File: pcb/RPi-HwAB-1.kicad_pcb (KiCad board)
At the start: 6 copper layers, 65 x 56 mm, 110 parts, among them J1 GPIO, J2 Hirose_FH12-16S, J3 TC2030, M1V0 TestPoint, M1V2 TestPoint, U1 CAT24C256, U2 ADP5054, U3 INA230AIRGTT, U4 MCP9804_DFN, U5 XC7A35T-FGG484, U6 INA230AIRGTT, U8 MX25L3233FZN

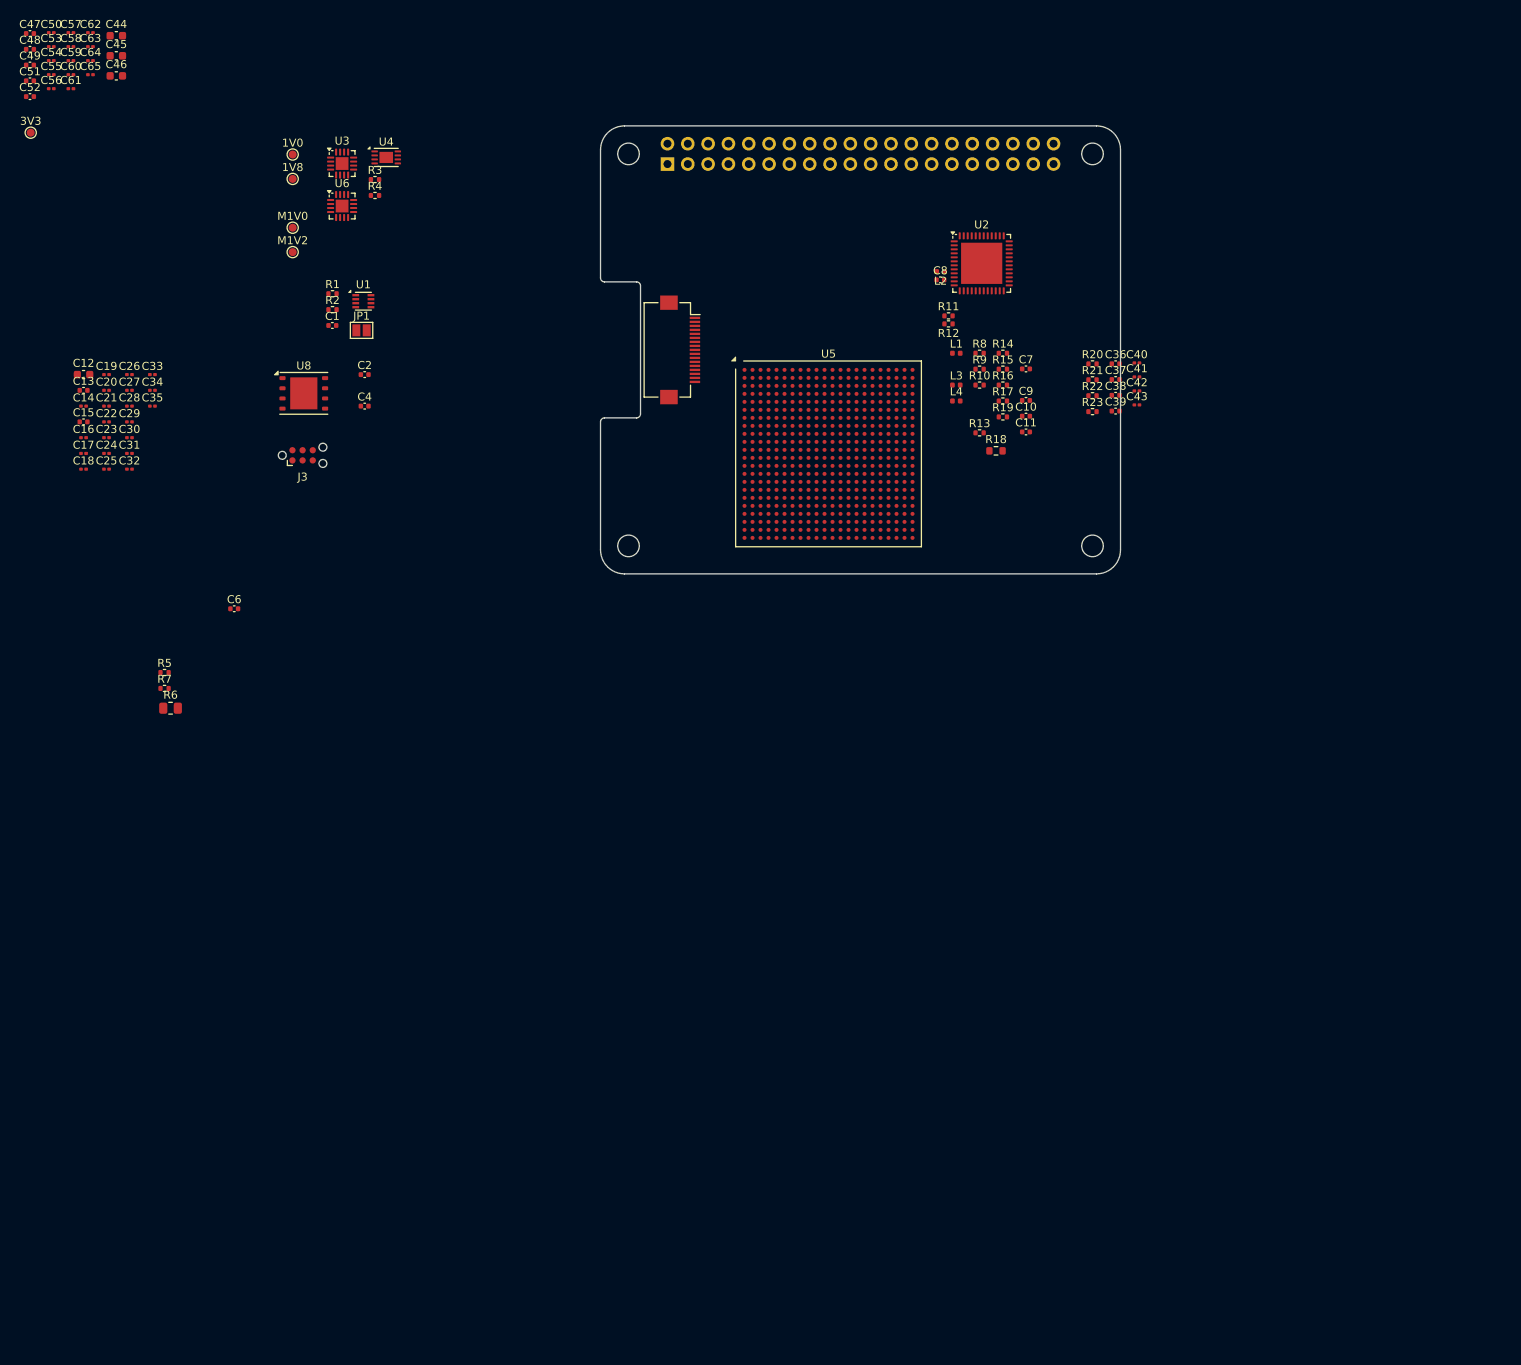
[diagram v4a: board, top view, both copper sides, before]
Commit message: defined memory pinouts
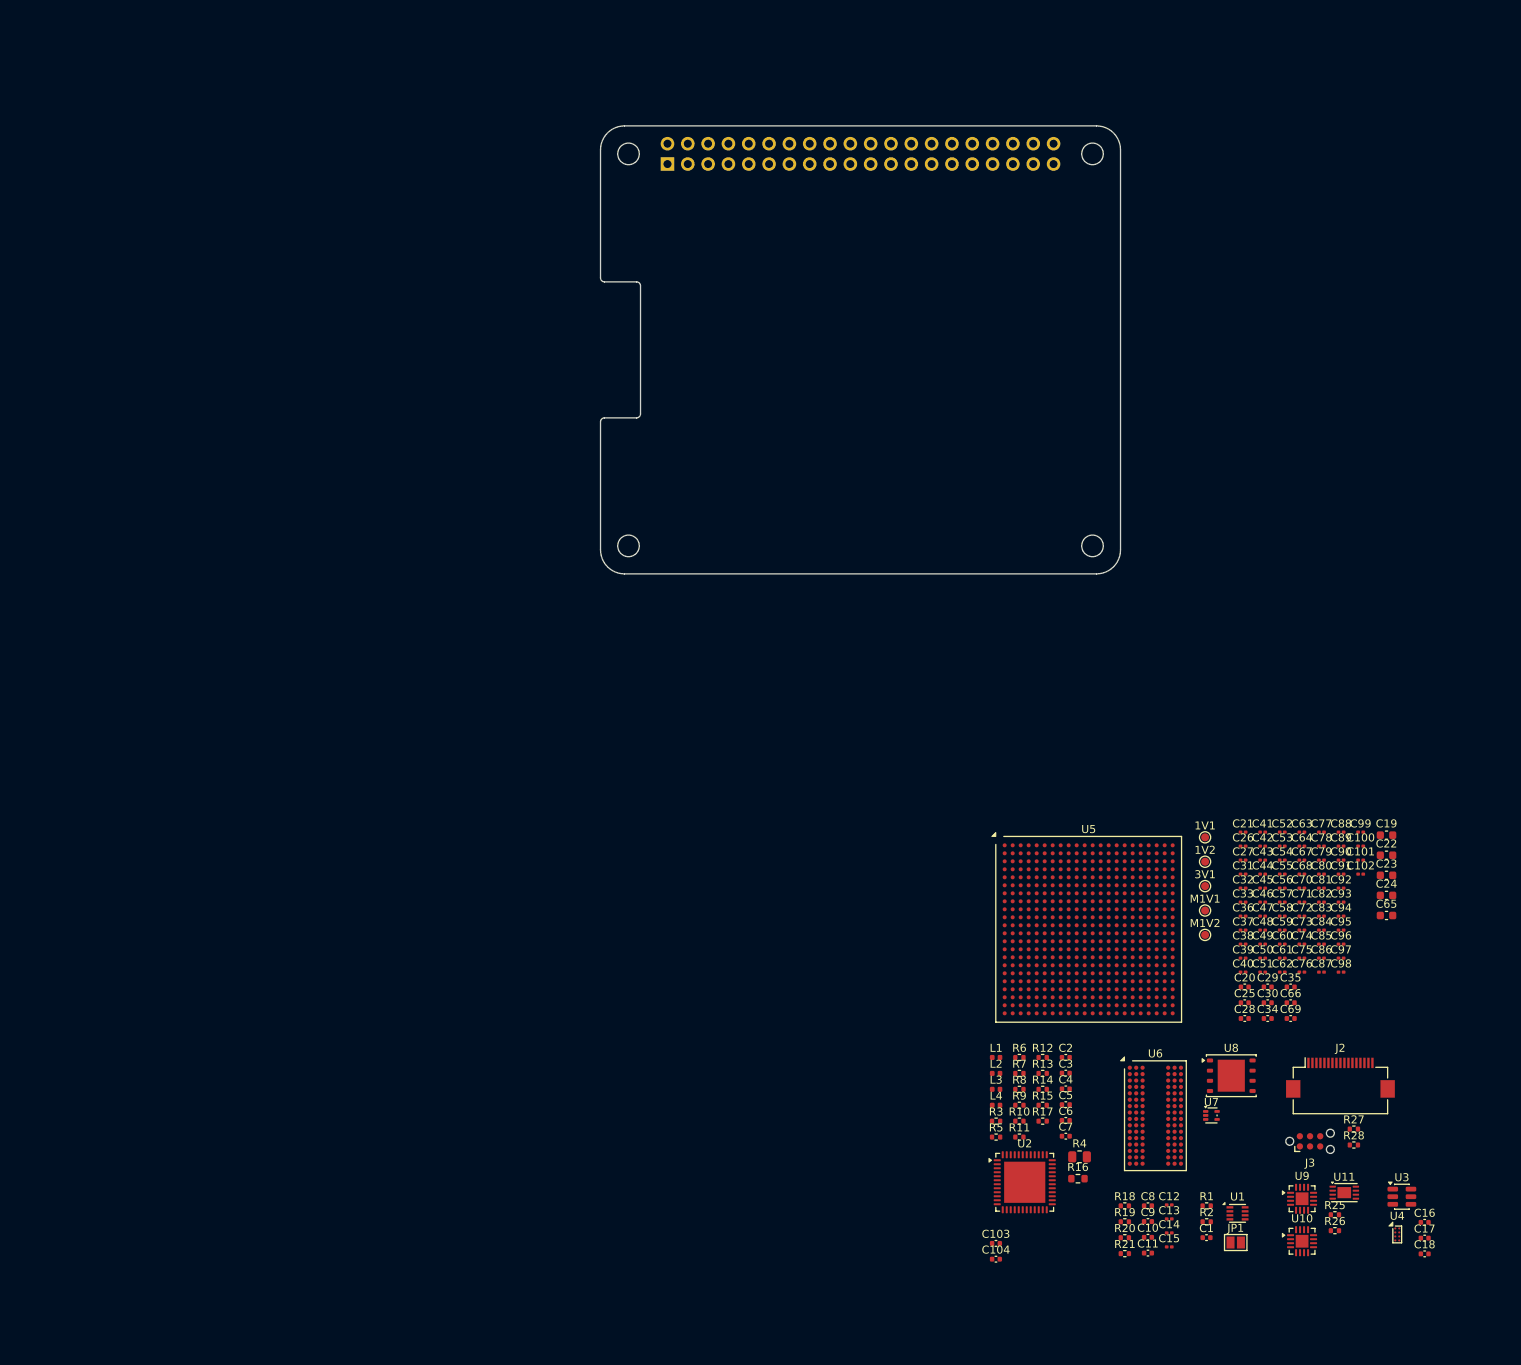
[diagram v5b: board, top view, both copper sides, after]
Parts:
- removed 1V0, 1V8, 3V3, M1V0: TestPoint, TestPoint:TestPoint_Pad_D1.0mm
- removed R22, R23: 10K, Resistor_SMD:R_0402_1005Metric
- added 1V1: TestPoint, TestPoint:TestPoint_Pad_D1.0mm, F.Cu at (175.6, 132.9)
- added 1V2: TestPoint, TestPoint:TestPoint_Pad_D1.0mm, F.Cu at (175.6, 136.0)
- added 3V1: TestPoint, TestPoint:TestPoint_Pad_D1.0mm, F.Cu at (175.6, 139.0)
- added C100: 0.1uF, Capacitor_SMD:C_0201_0603Metric, F.Cu at (195.0, 134.0)
- added C101: 0.1uF, Capacitor_SMD:C_0201_0603Metric, F.Cu at (195.0, 135.8)
- added C102: 0.1uF, Capacitor_SMD:C_0201_0603Metric, F.Cu at (195.0, 137.5)
- added C103: 0.1uF, Capacitor_SMD:C_0402_1005Metric, F.Cu at (149.4, 183.7)
- added C104: 0.1uF, Capacitor_SMD:C_0402_1005Metric, F.Cu at (149.4, 185.7)
- added C3: 0.1uF, Capacitor_SMD:C_0402_1005Metric, F.Cu at (158.2, 162.4)
- added C5: 0.1uF, Capacitor_SMD:C_0402_1005Metric, F.Cu at (158.2, 166.3)
- added C66: 0.1uF, Capacitor_SMD:C_0402_1005Metric, F.Cu at (186.3, 153.6)
- added C67: 0.1uF, Capacitor_SMD:C_0201_0603Metric, F.Cu at (187.7, 135.8)
- added C68: 0.1uF, Capacitor_SMD:C_0201_0603Metric, F.Cu at (187.7, 137.5)
- added C69: 10uF, Capacitor_SMD:C_0402_1005Metric, F.Cu at (186.3, 155.6)
- added C70: 0.1uF, Capacitor_SMD:C_0201_0603Metric, F.Cu at (187.7, 139.3)
- added C71: 0.1uF, Capacitor_SMD:C_0201_0603Metric, F.Cu at (187.7, 141.0)
- added C72: 0.1uF, Capacitor_SMD:C_0201_0603Metric, F.Cu at (187.7, 142.8)
- added C73: 0.1uF, Capacitor_SMD:C_0201_0603Metric, F.Cu at (187.7, 144.5)
- added C74: 0.1uF, Capacitor_SMD:C_0201_0603Metric, F.Cu at (187.7, 146.3)
- added C75: 0.1uF, Capacitor_SMD:C_0201_0603Metric, F.Cu at (187.7, 148.0)
- added C76: 0.1uF, Capacitor_SMD:C_0201_0603Metric, F.Cu at (187.7, 149.8)
- added C77: 0.1uF, Capacitor_SMD:C_0201_0603Metric, F.Cu at (190.1, 132.3)
- added C78: 0.1uF, Capacitor_SMD:C_0201_0603Metric, F.Cu at (190.1, 134.0)
- added C79: 0.1uF, Capacitor_SMD:C_0201_0603Metric, F.Cu at (190.1, 135.8)
- added C80: 0.1uF, Capacitor_SMD:C_0201_0603Metric, F.Cu at (190.1, 137.5)
- added C81: 0.1uF, Capacitor_SMD:C_0201_0603Metric, F.Cu at (190.1, 139.3)
- added C82: 0.1uF, Capacitor_SMD:C_0201_0603Metric, F.Cu at (190.1, 141.0)
- added C83: 0.1uF, Capacitor_SMD:C_0201_0603Metric, F.Cu at (190.1, 142.8)
- added C84: 0.1uF, Capacitor_SMD:C_0201_0603Metric, F.Cu at (190.1, 144.5)
- added C85: 0.1uF, Capacitor_SMD:C_0201_0603Metric, F.Cu at (190.1, 146.3)
- added C86: 0.1uF, Capacitor_SMD:C_0201_0603Metric, F.Cu at (190.1, 148.0)
- added C87: 0.1uF, Capacitor_SMD:C_0201_0603Metric, F.Cu at (190.1, 149.8)
- added C88: 0.1uF, Capacitor_SMD:C_0201_0603Metric, F.Cu at (192.6, 132.3)
- added C89: 0.1uF, Capacitor_SMD:C_0201_0603Metric, F.Cu at (192.6, 134.0)
- added C90: 0.1uF, Capacitor_SMD:C_0201_0603Metric, F.Cu at (192.6, 135.8)
- added C91: 0.1uF, Capacitor_SMD:C_0201_0603Metric, F.Cu at (192.6, 137.5)
- added C92: 0.1uF, Capacitor_SMD:C_0201_0603Metric, F.Cu at (192.6, 139.3)
- added C93: 0.1uF, Capacitor_SMD:C_0201_0603Metric, F.Cu at (192.6, 141.0)
- added C94: 0.1uF, Capacitor_SMD:C_0201_0603Metric, F.Cu at (192.6, 142.8)
- added C95: 0.1uF, Capacitor_SMD:C_0201_0603Metric, F.Cu at (192.6, 144.5)
- added C96: 0.1uF, Capacitor_SMD:C_0201_0603Metric, F.Cu at (192.6, 146.3)
- added C97: 0.1uF, Capacitor_SMD:C_0201_0603Metric, F.Cu at (192.6, 148.0)
- added C98: 0.1uF, Capacitor_SMD:C_0201_0603Metric, F.Cu at (192.6, 149.8)
- added C99: 0.1uF, Capacitor_SMD:C_0201_0603Metric, F.Cu at (195.0, 132.3)
- added M1V1: TestPoint, TestPoint:TestPoint_Pad_D1.0mm, F.Cu at (175.6, 142.1)
- added R25: 4.7K, Resistor_SMD:R_0402_1005Metric, F.Cu at (191.8, 180.1)
- added R26: 4.7K, Resistor_SMD:R_0402_1005Metric, F.Cu at (191.8, 182.1)
- added R27: 100K, Resistor_SMD:R_0402_1005Metric, F.Cu at (194.2, 169.4)
- added R28: 2.2K, Resistor_SMD:R_0402_1005Metric, F.Cu at (194.2, 171.4)
- added U10: INA230AIRGTT, Package_DFN_QFN:VQFN-16-1EP_3x3mm_P0.5mm_EP1.6x1.6mm, F.Cu at (187.7, 183.4)
- added U11: MCP9804_DFN, Package_DFN_QFN:DFN-8-1EP_3x2mm_P0.5mm_EP1.7x1.4mm, F.Cu at (193.0, 177.3)
- added U7: TCR2EE135, Package_TO_SOT_SMD:SOT-553, F.Cu at (176.4, 167.7)
- added U9: INA230AIRGTT, Package_DFN_QFN:VQFN-16-1EP_3x3mm_P0.5mm_EP1.6x1.6mm, F.Cu at (187.7, 178.1)
- C10, C11, C8, C9: value 0.1uF -> 10uF
- C12: value 47uF -> 2.2nF; footprint Capacitor_SMD:C_0603_1608Metric -> Capacitor_SMD:C_0201_0603Metric
- C13: value 0.1uF -> 2.2nF; footprint Capacitor_SMD:C_0402_1005Metric -> Capacitor_SMD:C_0201_0603Metric
- C14: value 0.1uF -> 2.2nF
- C15: value 10uF -> 2.2nF; footprint Capacitor_SMD:C_0402_1005Metric -> Capacitor_SMD:C_0201_0603Metric
- C16, C17, C18, C20, C30, C34, C35: footprint Capacitor_SMD:C_0201_0603Metric -> Capacitor_SMD:C_0402_1005Metric
- C19, C23, C24, C65: value 0.1uF -> 47uF; footprint Capacitor_SMD:C_0201_0603Metric -> Capacitor_SMD:C_0603_1608Metric
- C22: value 0.1uF -> 10uF; footprint Capacitor_SMD:C_0201_0603Metric -> Capacitor_SMD:C_0603_1608Metric
- C25, C28, C29: value 0.1uF -> 10uF; footprint Capacitor_SMD:C_0201_0603Metric -> Capacitor_SMD:C_0402_1005Metric
- C36, C37, C38, C39, C47, C48: value 10uF -> 0.1uF; footprint Capacitor_SMD:C_0402_1005Metric -> Capacitor_SMD:C_0201_0603Metric
- C40, C41, C42, C43: value 2.2nF -> 0.1uF
- C44: value 10uF -> 0.1uF; footprint Capacitor_SMD:C_0603_1608Metric -> Capacitor_SMD:C_0201_0603Metric
- C45, C46: value 47uF -> 0.1uF; footprint Capacitor_SMD:C_0603_1608Metric -> Capacitor_SMD:C_0201_0603Metric
- C49, C51, C52: footprint Capacitor_SMD:C_0402_1005Metric -> Capacitor_SMD:C_0201_0603Metric
- R11: value 75K -> 30K
- R12: value 24K -> 120K
- R13: value 30K -> 15K
- R14: value 120K -> 30K
- R15: value 15K -> 100
- R16: value 30K -> 0.005; footprint Resistor_SMD:R_0402_1005Metric -> Resistor_SMD:R_0603_1608Metric
- R18: value 0.005 -> 10K; footprint Resistor_SMD:R_0603_1608Metric -> Resistor_SMD:R_0402_1005Metric
- R19: value 100 -> 10K
- R3: value 4.7K -> 100
- R4: value 4.7K -> 0.003; footprint Resistor_SMD:R_0402_1005Metric -> Resistor_SMD:R_0805_2012Metric
- R6: value 0.003 -> 31.6K; footprint Resistor_SMD:R_0805_2012Metric -> Resistor_SMD:R_0402_1005Metric
- R7: value 100 -> 30K
- R8: value 31.6K -> 24K
- R9: value 30K -> 75K
- U3: value INA230AIRGTT -> LM3880; footprint Package_DFN_QFN:VQFN-16-1EP_3x3mm_P0.5mm_EP1.6x1.6mm -> Package_TO_SOT_SMD:SOT-23-6
- U4: value MCP9804_DFN -> TXS0102YZP; footprint Package_DFN_QFN:DFN-8-1EP_3x2mm_P0.5mm_EP1.7x1.4mm -> Package_BGA:Texas_DSBGA-8_0.9x1.9mm_Layout2x4_P0.5mm
- U5: value XC7A35T-FGG484 -> XC7A100T-FGG484; footprint Package_BGA:Xilinx_FGG484 -> library:Xilinx_FGG484
- U6: value INA230AIRGTT -> MT41K256M16LY; footprint Package_DFN_QFN:VQFN-16-1EP_3x3mm_P0.5mm_EP1.6x1.6mm -> Package_BGA:Micron_FBGA-96_7.5x13.5mm_Layout9x16_P0.8mm
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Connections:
- C10 pad 1: /Main Power/BST3 -> /Main Power/5V0_N
- C10 pad 2: /Main Power/SW3 -> GND
- C11 pad 1: /Main Power/1V0_SENS_P -> /Main Power/5V0_N
- C11 pad 2: /Main Power/1V0_SENS_N -> GND
- C12 pad 1: /FPGA/1V0_FD -> Net-(C12-Pad1)
- C13 pad 1: /FPGA/1V0_FD -> Net-(C13-Pad1)
- C14 pad 1: /FPGA/1V0_FD -> Net-(C14-Pad1)
- C15 pad 1: /FPGA/1V0_FD -> Net-(C15-Pad1)
- C16 pad 1: /FPGA/1V0_FD -> /Connectors/3V3
- C17 pad 1: /FPGA/1V0_FD -> /Main Power/5V0_N
- C18 pad 1: /FPGA/1V0_FD -> /Main Power/5V0_N
- C2 pad 1: /FPGA/FPGA 3/F2P_N -> /Main Power/5V0_SENS_P
- C2 pad 2: /Connectors/PCIE.F2P_N -> /Main Power/5V0_SENS_N
- C23 pad 1: /FPGA/1V0_FD -> /FPGA/1V2_MGT
- C24 pad 1: /FPGA/1V0_FD -> /FPGA/1V8_FD
- C28 pad 1: /FPGA/1V0_FD -> /FPGA/1V2_MGT
- C29 pad 1: /FPGA/1V0_FD -> /FPGA/1V8_FD
- C34 pad 1: /FPGA/1V0_FD -> /FPGA/1V2_MGT
- C35 pad 1: /FPGA/1V0_FD -> /FPGA/1V8_FD
- C36 pad 1: /Main Power/5V0_N -> /FPGA/1V0_FD
- C37 pad 1: /Main Power/5V0_N -> /FPGA/1V0_FD
- C38 pad 1: /Main Power/5V0_N -> /FPGA/1V0_FD
- C39 pad 1: /Main Power/5V0_N -> /FPGA/1V2_MGT
- C4 pad 1: /FPGA/FPGA 3/F2P_P -> /Main Power/BST4
- C4 pad 2: /Connectors/PCIE.F2P_P -> /Main Power/SW4
- C40 pad 1: Net-(C40-Pad1) -> /FPGA/1V8_FD
- C41 pad 1: Net-(C41-Pad1) -> /FPGA/1V0_FD
- C42 pad 1: Net-(C42-Pad1) -> /FPGA/1V0_FD
- C43 pad 1: Net-(C43-Pad1) -> /FPGA/1V0_FD
- C44 pad 1: /FPGA/1V0_FD -> /FPGA/1V2_MGT
- C45 pad 1: /FPGA/1V2_MGT -> /FPGA/1V8_FD
- C46 pad 1: /FPGA/1V8_FD -> /FPGA/1V0_FD
- C47 pad 1: /FPGA/1V2_MGT -> /FPGA/1V0_FD
- C48 pad 1: /FPGA/1V8_FD -> /FPGA/1V0_FD
- C49 pad 1: /FPGA/1V0_FD -> /FPGA/1V2_MGT
- C50 pad 1: /FPGA/1V0_FD -> /FPGA/1V8_FD
- C51 pad 1: /FPGA/1V2_MGT -> /FPGA/1V0_FD
- C52 pad 1: /FPGA/1V8_FD -> /FPGA/1V0_FD
- C53 pad 1: /FPGA/1V0_FD -> /FPGA/1V2_MGT
- C54 pad 1: /FPGA/1V2_MGT -> /FPGA/1V8_FD
- C55 pad 1: /FPGA/1V8_FD -> /FPGA/1V0_FD
- C6 pad 1: /Main Power/5V0_SENS_P -> /Main Power/BST3
- C6 pad 2: /Main Power/5V0_SENS_N -> /Main Power/SW3
- C60 pad 1: /FPGA/1V2_MGT -> /FPGA/1V0_FD
- C61 pad 1: /FPGA/1V8_FD -> /FPGA/1V0_FD
- C62 pad 1: /FPGA/1V2_MGT -> /FPGA/1V0_FD
- C63 pad 1: /FPGA/1V8_FD -> /FPGA/1V0_FD
- C64 pad 1: /FPGA/1V2_MGT -> /FPGA/1V0_FD
- C65 pad 1: /FPGA/1V8_FD -> GND
- C65 pad 2: GND -> Net-(C65-Pad2)
- C7 pad 1: /Main Power/BST2 -> /Main Power/1V0_SENS_P
- C7 pad 2: /Main Power/SW2 -> /Main Power/1V0_SENS_N
- C8 pad 1: /Main Power/BST4 -> /Main Power/5V0_N
- C8 pad 2: /Main Power/SW4 -> GND
- C9 pad 1: /Main Power/BST1 -> /Main Power/5V0_N
- C9 pad 2: /Main Power/SW1 -> GND
- J1 pad 10: /Connectors/EN2 -> unconnected-(J1-Pin_10-Pad10)
- J1 pad 12: /Connectors/EN3 -> unconnected-(J1-Pin_12-Pad12)
- J1 pad 16: /Connectors/EN4 -> unconnected-(J1-Pin_16-Pad16)
- J1 pad 8: /Connectors/EN1 -> unconnected-(J1-Pin_8-Pad8)
- J2 pad 15: /Connectors/PCIE.CLKREQ_N -> GND
- L2 pad 2: /FPGA/3V3_FD -> GND
- R10 pad 1: /Main Power/FB2 -> /Main Power/FB4
- R11 pad 1: /FPGA/3V3_FD -> /Main Power/1V0_P
- R11 pad 2: /Main Power/FB4 -> /Main Power/FB1
- R12 pad 1: /Main Power/FB4 -> /Main Power/FB1
- R13 pad 1: /Main Power/1V0_P -> /FPGA/1V2_MGT
- R13 pad 2: /Main Power/FB1 -> /Main Power/FB3
- R14 pad 1: /Main Power/FB1 -> /Main Power/FB3
- R15 pad 1: /FPGA/1V2_MGT -> /Main Power/1V0_SENS_N
- R15 pad 2: /Main Power/FB3 -> /Main Power/1V0_P
- R16 pad 1: /Main Power/FB3 -> /FPGA/1V0_FD
- R16 pad 2: GND -> /Main Power/1V0_P
- R17 pad 1: /Main Power/1V0_SENS_N -> /Main Power/1V0_SENS_P
- R17 pad 2: /Main Power/1V0_P -> /FPGA/1V0_FD
- R18 pad 1: /FPGA/1V0_FD -> Net-(C12-Pad1)
- R18 pad 2: /Main Power/1V0_P -> /Main Power/Comp & Decpl./COMP1
- R19 pad 1: /Main Power/1V0_SENS_P -> Net-(C13-Pad1)
- R19 pad 2: /FPGA/1V0_FD -> /Main Power/Comp & Decpl./COMP2
- R20 pad 1: Net-(C40-Pad1) -> Net-(C14-Pad1)
- R20 pad 2: /Main Power/Comp & Decpl./COMP1 -> /Main Power/Comp & Decpl./COMP3
- R21 pad 1: Net-(C41-Pad1) -> Net-(C15-Pad1)
- R21 pad 2: /Main Power/Comp & Decpl./COMP2 -> /Main Power/Comp & Decpl./COMP4
- R3 pad 1: /Connectors/3V3 -> /Main Power/5V0_SENS_P
- R3 pad 2: /Connectors/I2C1.SDA -> /Connectors/5V0
- R4 pad 1: /Connectors/3V3 -> /Connectors/5V0
- R4 pad 2: /Connectors/I2C1.SCL -> /Main Power/5V0_N
- R5 pad 1: /Main Power/5V0_SENS_P -> /Main Power/5V0_SENS_N
- R5 pad 2: /Connectors/5V0 -> /Main Power/5V0_N
- R6 pad 1: /Connectors/5V0 -> GND
- R6 pad 2: /Main Power/5V0_N -> Net-(U2-RT)
- R7 pad 1: /Main Power/5V0_SENS_N -> /FPGA/1V8_FD
- R7 pad 2: /Main Power/5V0_N -> /Main Power/FB2
- R8 pad 1: GND -> /Main Power/FB2
- R8 pad 2: Net-(U2-RT) -> GND
- R9 pad 1: /FPGA/1V8_FD -> GND
- R9 pad 2: /Main Power/FB2 -> /Main Power/FB4
- U2 pad 14: /Connectors/EN4 -> /Main Power/EN4
- U2 pad 21: /Connectors/EN2 -> /Main Power/EN2
- U2 pad 39: /Connectors/EN1 -> /Main Power/EN1
- U2 pad 48: /Connectors/EN3 -> /Main Power/EN3
- U3 pad 1: GND -> /Main Power/5V0_N
- U3 pad 3: unconnected-(U3-ALERT-Pad3) -> /Main Power/EN1
- U3 pad 4: /Connectors/I2C1.SDA -> /Main Power/EN4
- U3 pad 5: /Connectors/I2C1.SCL -> /Main Power/EN3
- U3 pad 6: GND -> /Main Power/EN2
- U5 pad A11: GND -> unconnected-(U5I-GND-PadA11)
- U5 pad A12: GND -> unconnected-(U5I-GND-PadA12)
- U5 pad A17: /FPGA/3V3_FD -> unconnected-(U5D-VCCO_16-PadA17)
- U5 pad A2: GND -> unconnected-(U5I-GND-PadA2)
- U5 pad A22: GND -> unconnected-(U5I-GND-PadA22)
- U5 pad A3: GND -> unconnected-(U5I-GND-PadA3)
- U5 pad A4: /FPGA/FPGA 3/F2P_N -> /FPGA/FPGA 4/F2P_N
- U5 pad A5: GND -> unconnected-(U5I-GND-PadA5)
- U5 pad A7: GND -> unconnected-(U5I-GND-PadA7)
- U5 pad A8: /Connectors/PCIE.P2F_N -> /FPGA/FPGA 4/PCIE.P2F_N
- U5 pad A9: GND -> unconnected-(U5I-GND-PadA9)
- U5 pad AA10: (no net) -> unconnected-(U5A-IO_L9P_T1_DQS_13-PadAA10)
- U5 pad AA11: (no net) -> unconnected-(U5A-IO_L9N_T1_DQS_13-PadAA11)
- U5 pad AA12: GND -> unconnected-(U5I-GND-PadAA12)
- U5 pad AA13: (no net) -> unconnected-(U5A-IO_L3P_T0_DQS_13-PadAA13)
- U5 pad AA14: (no net) -> unconnected-(U5A-IO_L5N_T0_13-PadAA14)
- U5 pad AA15: (no net) -> unconnected-(U5A-IO_L4P_T0_13-PadAA15)
- U5 pad AA16: (no net) -> unconnected-(U5A-IO_L1N_T0_13-PadAA16)
- U5 pad AA17: /FPGA/3V3_FD -> unconnected-(U5A-VCCO_13-PadAA17)
- U5 pad AA2: GND -> unconnected-(U5I-GND-PadAA2)
- U5 pad AA22: GND -> unconnected-(U5I-GND-PadAA22)
- U5 pad AA7: /FPGA/3V3_FD -> unconnected-(U5E-VCCO_34-PadAA7)
- U5 pad AA9: (no net) -> unconnected-(U5A-IO_L8P_T1_13-PadAA9)
- U5 pad AB10: (no net) -> unconnected-(U5A-IO_L8N_T1_13-PadAB10)
- U5 pad AB11: (no net) -> unconnected-(U5A-IO_L7P_T1_13-PadAB11)
- U5 pad AB12: (no net) -> unconnected-(U5A-IO_L7N_T1_13-PadAB12)
- U5 pad AB13: (no net) -> unconnected-(U5A-IO_L3N_T0_DQS_13-PadAB13)
- U5 pad AB14: /FPGA/3V3_FD -> unconnected-(U5A-VCCO_13-PadAB14)
- U5 pad AB15: (no net) -> unconnected-(U5A-IO_L4N_T0_13-PadAB15)
- U5 pad AB16: (no net) -> unconnected-(U5A-IO_L2P_T0_13-PadAB16)
- U5 pad AB17: (no net) -> unconnected-(U5A-IO_L2N_T0_13-PadAB17)
- U5 pad AB19: GND -> unconnected-(U5I-GND-PadAB19)
- U5 pad AB4: /FPGA/3V3_FD -> unconnected-(U5E-VCCO_34-PadAB4)
- U5 pad AB9: GND -> unconnected-(U5I-GND-PadAB9)
- U5 pad B11: /FPGA/1V2_MGT -> unconnected-(U5G-MGTAVTT-PadB11)
- U5 pad B12: GND -> unconnected-(U5I-GND-PadB12)
- U5 pad B14: /FPGA/3V3_FD -> unconnected-(U5D-VCCO_16-PadB14)
- U5 pad B19: GND -> unconnected-(U5I-GND-PadB19)
- U5 pad B3: GND -> unconnected-(U5I-GND-PadB3)
- U5 pad B4: /FPGA/FPGA 3/F2P_P -> /FPGA/FPGA 4/F2P_P
- U5 pad B5: /FPGA/1V2_MGT -> unconnected-(U5G-MGTAVTT-PadB5)
- U5 pad B7: /FPGA/1V2_MGT -> unconnected-(U5G-MGTAVTT-PadB7)
- U5 pad B8: /Connectors/PCIE.P2F_P -> /FPGA/FPGA 4/PCIE.P2F_P
- U5 pad B9: /FPGA/1V2_MGT -> unconnected-(U5G-MGTAVTT-PadB9)
- U5 pad C1: /FPGA/3V3_FD -> unconnected-(U5F-VCCO_35-PadC1)
- U5 pad C10: GND -> unconnected-(U5I-GND-PadC10)
- U5 pad C12: GND -> unconnected-(U5I-GND-PadC12)
- U5 pad C16: GND -> unconnected-(U5I-GND-PadC16)
- U5 pad C21: /FPGA/3V3_FD -> unconnected-(U5D-VCCO_16-PadC21)
- U5 pad C3: GND -> unconnected-(U5I-GND-PadC3)
- U5 pad C4: /FPGA/1V2_MGT -> unconnected-(U5G-MGTAVTT-PadC4)
- U5 pad C6: GND -> unconnected-(U5I-GND-PadC6)
- U5 pad C8: /FPGA/1V2_MGT -> unconnected-(U5G-MGTAVTT-PadC8)
- U5 pad D10: /FPGA/1V0_FD -> unconnected-(U5G-MGTAVCC-PadD10)
- U5 pad D12: GND -> unconnected-(U5I-GND-PadD12)
- U5 pad D13: GND -> unconnected-(U5I-GND-PadD13)
- U5 pad D18: /FPGA/3V3_FD -> unconnected-(U5D-VCCO_16-PadD18)
- U5 pad D3: GND -> unconnected-(U5I-GND-PadD3)
- U5 pad D4: GND -> unconnected-(U5I-GND-PadD4)
- U5 pad D6: /FPGA/1V0_FD -> unconnected-(U5G-MGTAVCC-PadD6)
- U5 pad D8: GND -> unconnected-(U5I-GND-PadD8)
- U5 pad E11: GND -> unconnected-(U5I-GND-PadE11)
- U5 pad E12: GND -> unconnected-(U5I-VCCBATT_0-PadE12)
- U5 pad E15: /FPGA/3V3_FD -> unconnected-(U5D-VCCO_16-PadE15)
- U5 pad E20: GND -> unconnected-(U5I-GND-PadE20)
- U5 pad E4: GND -> unconnected-(U5I-GND-PadE4)
- U5 pad E5: GND -> unconnected-(U5I-GND-PadE5)
- U5 pad E6: /Connectors/PCIE.CLK_N -> /FPGA/FPGA 4/PCIE.CLK_N
- U5 pad E7: GND -> unconnected-(U5I-GND-PadE7)
- U5 pad E8: /FPGA/1V0_FD -> unconnected-(U5G-MGTAVCC-PadE8)
- U5 pad E9: GND -> unconnected-(U5I-GND-PadE9)
- U5 pad F11: GND -> unconnected-(U5I-GND-PadF11)
- U5 pad F12: /FPGA/3V3_FD -> unconnected-(U5H-VCCO_0-PadF12)
- U5 pad F17: GND -> unconnected-(U5I-GND-PadF17)
- U5 pad F2: /FPGA/3V3_FD -> unconnected-(U5F-VCCO_35-PadF2)
- U5 pad F22: /FPGA/3V3_FD -> unconnected-(U5D-VCCO_16-PadF22)
- U5 pad F5: GND -> unconnected-(U5I-GND-PadF5)
- U5 pad F6: /Connectors/PCIE.CLK_P -> /FPGA/FPGA 4/PCIE.CLK_P
- U5 pad F7: /FPGA/1V0_FD -> unconnected-(U5G-MGTAVCC-PadF7)
- U5 pad F9: /FPGA/1V0_FD -> unconnected-(U5G-MGTAVCC-PadF9)
- U5 pad G10: GND -> unconnected-(U5I-GND-PadG10)
- U5 pad G12: GND -> unconnected-(U5I-GND-PadG12)
- U5 pad G14: GND -> unconnected-(U5I-GND-PadG14)
- U5 pad G19: /FPGA/3V3_FD -> unconnected-(U5C-VCCO_15-PadG19)
- U5 pad G5: GND -> unconnected-(U5I-GND-PadG5)
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
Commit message: power restructuring
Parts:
- removed C11: 10uF, Capacitor_SMD:C_0402_1005Metric
- removed C12, C13, C14, C15: 2.2nF, Capacitor_SMD:C_0201_0603Metric
- removed C16, C17, C18, C3, C4, C5, C6: 0.1uF, Capacitor_SMD:C_0402_1005Metric
- removed L1, L2, L3, L4: 1uH, Inductor_SMD:L_0402_1005Metric
- removed R10, R8: 24K, Resistor_SMD:R_0402_1005Metric
- removed R11, R14, R7: 30K, Resistor_SMD:R_0402_1005Metric
- removed R12: 120K, Resistor_SMD:R_0402_1005Metric
- removed R13: 15K, Resistor_SMD:R_0402_1005Metric
- removed R18, R19, R20, R21: 10K, Resistor_SMD:R_0402_1005Metric
- removed R6: 31.6K, Resistor_SMD:R_0402_1005Metric
- removed R9: 75K, Resistor_SMD:R_0402_1005Metric
- added C105: 0.1uF, Capacitor_SMD:C_0201_0603Metric, F.Cu at (173.8, 194.3)
- added C106: 0.1uF, Capacitor_SMD:C_0201_0603Metric, F.Cu at (173.8, 196.1)
- added R30: 4.7K, Resistor_SMD:R_0402_1005Metric, F.Cu at (174.0, 190.4)
- added R31: 4.7K, Resistor_SMD:R_0402_1005Metric, F.Cu at (174.0, 192.4)
- added U12: TPSM82903, library:TPSM82903SISR, F.Cu at (199.8, 177.7)
- added U13: TPSM82903, library:TPSM82903SISR, F.Cu at (199.8, 182.3)
- added U14: AP3441SHE-7B, Package_DFN_QFN:DFN-8-1EP_2x2mm_P0.5mm_EP1.05x1.75mm, F.Cu at (207.1, 176.8)
- added Y1: SiT9365AI-2B2-33E200.000000, Oscillator:Oscillator_SMD_SiTime_PQFD-6L_3.2x2.5mm, F.Cu at (170.4, 191.9)
- C10, C8, C9: value 10uF -> 0.1uF
- U2: value ADP5054 -> TPSM82903; footprint Package_DFN_QFN:QFN-48-1EP_7x7mm_P0.5mm_EP5.15x5.15mm -> library:TPSM82903SISR
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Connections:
- C10 pad 1: /Main Power/5V0_N -> /Main Power/Sequencing/5V0
- C103 pad 2: /FPGA/FPGA 4/PCIE.F2P_N -> /Connectors/PCIE.F2P_P
- C104 pad 2: /FPGA/FPGA 4/PCIE.F2P_P -> /Connectors/PCIE.F2P_N
- C8 pad 1: /Main Power/5V0_N -> /Main Power/Sequencing/3V3
- C9 pad 1: /Main Power/5V0_N -> /Main Power/Sequencing/5V0
- R16 pad 1: /FPGA/1V0_FD -> Net-(R16-Pad1)
- R17 pad 2: /FPGA/1V0_FD -> Net-(R16-Pad1)
- R4 pad 2: /Main Power/5V0_N -> Net-(R4-Pad2)
- R5 pad 2: /Main Power/5V0_N -> Net-(R4-Pad2)
- U2 pad 1: /Main Power/BST3 -> Net-(U2-MODE)
- U2 pad 10: GND -> Net-(C4-Pad1)
- U2 pad 12: /Main Power/BST4 -> (no net)
- U2 pad 13: unconnected-(U2-CFG34-Pad13) -> (no net)
- U2 pad 14: /Main Power/EN4 -> (no net)
- U2 pad 2: GND -> Net-(U2-MODE)
- U2 pad 3: GND -> /Connectors/PCIE.PWR_EN
- U2 pad 4: /Main Power/SW3 -> Net-(U2-MODE)
- U2 pad 5: /Main Power/SW3 -> unconnected-(U2-SS/TR-Pad5)
- U2 pad 6: /Main Power/5V0_N -> Net-(U12-EN)
- U2 pad 7: /Main Power/5V0_N -> Net-(U2-FB/VSET)
- U2 pad 8: /Main Power/SW4 -> unconnected-(U2-SW-Pad8)
- U2 pad 9: /Main Power/SW4 -> Net-(C4-Pad1)
- U3 pad 1: /Main Power/5V0_N -> /Main Power/Sequencing/5V0
- U3 pad 3: /Main Power/EN1 -> /Main Power/Sequencing/EN1
- U3 pad 4: /Main Power/EN4 -> /Main Power/Sequencing/EN4
- U3 pad 5: /Main Power/EN3 -> /Main Power/Sequencing/EN3
- U3 pad 6: /Main Power/EN2 -> /Main Power/Sequencing/EN2
- U4 pad A2: /Main Power/EN1 -> /Main Power/Sequencing/EN1
- U4 pad B2: /Main Power/5V0_N -> /Main Power/Sequencing/5V0
- U4 pad C1: /Connectors/3V3 -> /Main Power/Sequencing/3V3
- U4 pad D2: /Connectors/PCIE.PWR_EN -> /Main Power/Sequencing/PCIE.PWR_EN
- U5 pad A1: unconnected-(U5F-IO_L1N_T0_AD4N_35-PadA1) -> /FPGA/FPGA 3/DQ1
- U5 pad A11: unconnected-(U5I-GND-PadA11) -> GND
- U5 pad A12: unconnected-(U5I-GND-PadA12) -> GND
- U5 pad A2: unconnected-(U5I-GND-PadA2) -> GND
- U5 pad A22: unconnected-(U5I-GND-PadA22) -> GND
- U5 pad A3: unconnected-(U5I-GND-PadA3) -> GND
- U5 pad A5: unconnected-(U5I-GND-PadA5) -> GND
- U5 pad A7: unconnected-(U5I-GND-PadA7) -> GND
- U5 pad A8: /FPGA/FPGA 4/PCIE.P2F_N -> /Connectors/PCIE.P2F_P
- U5 pad A9: unconnected-(U5I-GND-PadA9) -> GND
- U5 pad AA12: unconnected-(U5I-GND-PadAA12) -> GND
- U5 pad AA2: unconnected-(U5I-GND-PadAA2) -> GND
- U5 pad AA22: unconnected-(U5I-GND-PadAA22) -> GND
- U5 pad AA7: unconnected-(U5E-VCCO_34-PadAA7) -> /FPGA/FPGA 3/1V35_FD
- U5 pad AB19: unconnected-(U5I-GND-PadAB19) -> GND
- U5 pad AB4: unconnected-(U5E-VCCO_34-PadAB4) -> /FPGA/FPGA 3/1V35_FD
- U5 pad AB9: unconnected-(U5I-GND-PadAB9) -> GND
- U5 pad B1: unconnected-(U5F-IO_L1P_T0_AD4P_35-PadB1) -> /FPGA/FPGA 3/DQ0
- U5 pad B11: unconnected-(U5G-MGTAVTT-PadB11) -> /FPGA/FPGA 4/1V2_MGT
- U5 pad B12: unconnected-(U5I-GND-PadB12) -> GND
- U5 pad B19: unconnected-(U5I-GND-PadB19) -> GND
- U5 pad B2: unconnected-(U5F-IO_L2N_T0_AD12N_35-PadB2) -> /FPGA/FPGA 3/DQ3
- U5 pad B3: unconnected-(U5I-GND-PadB3) -> GND
- U5 pad B5: unconnected-(U5G-MGTAVTT-PadB5) -> /FPGA/FPGA 4/1V2_MGT
- U5 pad B7: unconnected-(U5G-MGTAVTT-PadB7) -> /FPGA/FPGA 4/1V2_MGT
- U5 pad B8: /FPGA/FPGA 4/PCIE.P2F_P -> /Connectors/PCIE.P2F_N
- U5 pad B9: unconnected-(U5G-MGTAVTT-PadB9) -> /FPGA/FPGA 4/1V2_MGT
- U5 pad C1: unconnected-(U5F-VCCO_35-PadC1) -> /FPGA/FPGA 3/1V35_FD
- U5 pad C10: unconnected-(U5I-GND-PadC10) -> GND
- U5 pad C12: unconnected-(U5I-GND-PadC12) -> GND
- U5 pad C16: unconnected-(U5I-GND-PadC16) -> GND
- U5 pad C2: unconnected-(U5F-IO_L2P_T0_AD12P_35-PadC2) -> /FPGA/FPGA 3/DQ2
- U5 pad C3: unconnected-(U5I-GND-PadC3) -> GND
- U5 pad C4: unconnected-(U5G-MGTAVTT-PadC4) -> /FPGA/FPGA 4/1V2_MGT
- U5 pad C6: unconnected-(U5I-GND-PadC6) -> GND
- U5 pad C8: unconnected-(U5G-MGTAVTT-PadC8) -> /FPGA/FPGA 4/1V2_MGT
- U5 pad D1: unconnected-(U5F-IO_L3N_T0_DQS_AD5N_35-PadD1) -> /FPGA/FPGA 3/LDQS_N
- U5 pad D10: unconnected-(U5G-MGTAVCC-PadD10) -> /FPGA/FPGA 4/1V0_MGT
- U5 pad D12: unconnected-(U5I-GND-PadD12) -> GND
- U5 pad D13: unconnected-(U5I-GND-PadD13) -> GND
- U5 pad D2: unconnected-(U5F-IO_L4N_T0_35-PadD2) -> /FPGA/FPGA 3/DQ5
- U5 pad D3: unconnected-(U5I-GND-PadD3) -> GND
- U5 pad D4: unconnected-(U5I-GND-PadD4) -> GND
- U5 pad D6: unconnected-(U5G-MGTAVCC-PadD6) -> /FPGA/FPGA 4/1V0_MGT
- U5 pad D8: unconnected-(U5I-GND-PadD8) -> GND
- U5 pad E1: unconnected-(U5F-IO_L3P_T0_DQS_AD5P_35-PadE1) -> /FPGA/FPGA 3/LDQS_P
- U5 pad E11: unconnected-(U5I-GND-PadE11) -> GND
- U5 pad E2: unconnected-(U5F-IO_L4P_T0_35-PadE2) -> /FPGA/FPGA 3/DQ4
- U5 pad E20: unconnected-(U5I-GND-PadE20) -> GND
- U5 pad E4: unconnected-(U5I-GND-PadE4) -> GND
- U5 pad E5: unconnected-(U5I-GND-PadE5) -> GND
- U5 pad E6: /FPGA/FPGA 4/PCIE.CLK_N -> /Connectors/PCIE.CLK_P
- U5 pad E7: unconnected-(U5I-GND-PadE7) -> GND
- U5 pad E8: unconnected-(U5G-MGTAVCC-PadE8) -> /FPGA/FPGA 4/1V0_MGT
- U5 pad E9: unconnected-(U5I-GND-PadE9) -> GND
- U5 pad F1: unconnected-(U5F-IO_L5N_T0_AD13N_35-PadF1) -> /FPGA/FPGA 3/DQ7
- U5 pad F11: unconnected-(U5I-GND-PadF11) -> GND
- U5 pad F17: unconnected-(U5I-GND-PadF17) -> GND
- U5 pad F2: unconnected-(U5F-VCCO_35-PadF2) -> /FPGA/FPGA 3/1V35_FD
- U5 pad F3: unconnected-(U5F-IO_L6P_T0_35-PadF3) -> /FPGA/FPGA 3/LDM
- U5 pad F5: unconnected-(U5I-GND-PadF5) -> GND
- U5 pad F6: /FPGA/FPGA 4/PCIE.CLK_P -> /Connectors/PCIE.CLK_N
- U5 pad F7: unconnected-(U5G-MGTAVCC-PadF7) -> /FPGA/FPGA 4/1V0_MGT
- U5 pad F8: unconnected-(U5G-MGTRREF_216-PadF8) -> Net-(U5G-MGTRREF_216)
- U5 pad F9: unconnected-(U5G-MGTAVCC-PadF9) -> /FPGA/FPGA 4/1V0_MGT
- U5 pad G1: unconnected-(U5F-IO_L5P_T0_AD13P_35-PadG1) -> /FPGA/FPGA 3/DQ6
- U5 pad G10: unconnected-(U5I-GND-PadG10) -> GND
- U5 pad G12: unconnected-(U5I-GND-PadG12) -> GND
- U5 pad G14: unconnected-(U5I-GND-PadG14) -> GND
- U5 pad G2: unconnected-(U5F-IO_L8N_T1_AD14N_35-PadG2) -> /FPGA/FPGA 3/DQ11
- U5 pad G3: unconnected-(U5F-IO_L11N_T1_SRCC_35-PadG3) -> /FPGA/FPGA 3/DQ15
- U5 pad G5: unconnected-(U5I-GND-PadG5) -> GND
- U5 pad G6: unconnected-(U5I-GND-PadG6) -> GND
- U5 pad G7: unconnected-(U5I-GND-PadG7) -> GND
- U5 pad G8: unconnected-(U5I-GND-PadG8) -> GND
- U5 pad G9: unconnected-(U5I-GND-PadG9) -> GND
- U5 pad H1: unconnected-(U5I-GND-PadH1) -> GND
- U5 pad H11: unconnected-(U5I-GND-PadH11) -> GND
- U5 pad H2: unconnected-(U5F-IO_L8P_T1_AD14P_35-PadH2) -> /FPGA/FPGA 3/DQ10
- U5 pad H21: unconnected-(U5I-GND-PadH21) -> GND
- U5 pad H3: unconnected-(U5F-IO_L11P_T1_SRCC_35-PadH3) -> /FPGA/FPGA 3/DQ14
- U5 pad H4: unconnected-(U5F-IO_L12P_T1_MRCC_35-PadH4) -> /FPGA/FPGA 3/UDM
- U5 pad H5: unconnected-(U5F-IO_L10N_T1_AD15N_35-PadH5) -> /FPGA/FPGA 3/DQ13
- U5 pad H6: unconnected-(U5F-VCCO_35-PadH6) -> /FPGA/FPGA 3/1V35_FD
- U5 pad H7: unconnected-(U5I-GND-PadH7) -> GND
- U5 pad H9: unconnected-(U5I-GND-PadH9) -> GND
- U5 pad J1: unconnected-(U5F-IO_L7N_T1_AD6N_35-PadJ1) -> /FPGA/FPGA 3/DQ9
- U5 pad J10: unconnected-(U5I-GND-PadJ10) -> GND
- U5 pad J12: unconnected-(U5I-GND-PadJ12) -> GND
- U5 pad J18: unconnected-(U5I-GND-PadJ18) -> GND
- U5 pad J2: unconnected-(U5F-IO_L9N_T1_DQS_AD7N_35-PadJ2) -> /FPGA/FPGA 3/UDQS_N
- U5 pad J3: unconnected-(U5F-VCCO_35-PadJ3) -> /FPGA/FPGA 3/1V35_FD
- U5 pad J4: unconnected-(U5F-IO_L13N_T2_MRCC_35-PadJ4) -> /FPGA/FPGA 3/A1
- U5 pad J5: unconnected-(U5F-IO_L10P_T1_AD15P_35-PadJ5) -> /FPGA/FPGA 3/DQ12
- U5 pad J6: unconnected-(U5F-IO_L17N_T2_35-PadJ6) -> /FPGA/FPGA 3/A9
- U5 pad J8: unconnected-(U5I-GND-PadJ8) -> GND
- U5 pad K1: unconnected-(U5F-IO_L7P_T1_AD6P_35-PadK1) -> /FPGA/FPGA 3/DQ8
- U5 pad K11: unconnected-(U5I-GND-PadK11) -> GND
- U5 pad K15: unconnected-(U5I-GND-PadK15) -> GND
- U5 pad K2: unconnected-(U5F-IO_L9P_T1_DQS_AD7P_35-PadK2) -> /FPGA/FPGA 3/UDQS_P
- U5 pad K3: unconnected-(U5F-IO_L14N_T2_SRCC_35-PadK3) -> /FPGA/FPGA 3/A3
- U5 pad K4: unconnected-(U5F-IO_L13P_T2_MRCC_35-PadK4) -> /FPGA/FPGA 3/A0
- U5 pad K5: unconnected-(U5I-GND-PadK5) -> GND
- U5 pad K6: unconnected-(U5F-IO_L17P_T2_35-PadK6) -> /FPGA/FPGA 3/A8
- U5 pad K7: unconnected-(U5I-GND-PadK7) -> GND
- U5 pad L1: unconnected-(U5F-IO_L15N_T2_DQS_35-PadL1) -> /FPGA/FPGA 3/A5
- U5 pad L2: unconnected-(U5I-GND-PadL2) -> GND
- U5 pad L22: unconnected-(U5I-GND-PadL22) -> GND
- U5 pad L3: unconnected-(U5F-IO_L14P_T2_SRCC_35-PadL3) -> /FPGA/FPGA 3/A2
- U5 pad L4: unconnected-(U5F-IO_L18N_T2_35-PadL4) -> /FPGA/FPGA 3/A11
- U5 pad L5: unconnected-(U5F-IO_L18P_T2_35-PadL5) -> /FPGA/FPGA 3/A10
- U5 pad L8: unconnected-(U5I-GND-PadL8) -> GND
- U5 pad M1: unconnected-(U5F-IO_L15P_T2_DQS_35-PadM1) -> /FPGA/FPGA 3/A4
- U5 pad M11: unconnected-(U5I-GND-PadM11) -> GND
- U5 pad M19: unconnected-(U5I-GND-PadM19) -> GND
- U5 pad M2: unconnected-(U5F-IO_L16N_T2_35-PadM2) -> /FPGA/FPGA 3/A7
- U5 pad M3: unconnected-(U5F-IO_L16P_T2_35-PadM3) -> /FPGA/FPGA 3/A6
- U5 pad M4: unconnected-(U5F-VCCO_35-PadM4) -> /FPGA/FPGA 3/1V35_FD
- U5 pad M5: unconnected-(U5F-IO_L23N_T3_35-PadM5) -> /FPGA/FPGA 3/CKE
- U5 pad M6: unconnected-(U5F-IO_L23P_T3_35-PadM6) -> /FPGA/FPGA 3/ODT
- U5 pad M7: unconnected-(U5I-GND-PadM7) -> GND
- U5 pad N1: unconnected-(U5F-VCCO_35-PadN1) -> /FPGA/FPGA 3/1V35_FD
- U5 pad N16: unconnected-(U5I-GND-PadN16) -> GND
- U5 pad N2: unconnected-(U5F-IO_L22N_T3_35-PadN2) -> /FPGA/FPGA 3/WEn
- U5 pad N3: unconnected-(U5F-IO_L19N_T3_VREF_35-PadN3) -> /FPGA/FPGA 3/BA0
- U5 pad N4: unconnected-(U5F-IO_L19P_T3_35-PadN4) -> /FPGA/FPGA 3/A12
- U5 pad N5: unconnected-(U5F-IO_L24N_T3_35-PadN5) -> /FPGA/FPGA 3/CKn
- U5 pad N6: unconnected-(U5I-GND-PadN6) -> GND
- U5 pad N8: unconnected-(U5I-GND-PadN8) -> GND
- U5 pad P1: unconnected-(U5F-IO_L20N_T3_35-PadP1) -> /FPGA/FPGA 3/BA2
- U5 pad P11: unconnected-(U5I-GND-PadP11) -> GND
- U5 pad P13: unconnected-(U5I-GND-PadP13) -> GND
- U5 pad P2: unconnected-(U5F-IO_L22P_T3_35-PadP2) -> /FPGA/FPGA 3/CASn
- U5 pad P3: unconnected-(U5I-GND-PadP3) -> GND
- U5 pad P4: unconnected-(U5F-IO_L21N_T3_DQS_35-PadP4) -> /FPGA/FPGA 3/RASn
- U5 pad P5: unconnected-(U5F-IO_L21P_T3_DQS_35-PadP5) -> /FPGA/FPGA 3/CSn
- U5 pad P6: unconnected-(U5F-IO_L24P_T3_35-PadP6) -> /FPGA/FPGA 3/CKp
- U5 pad P7: unconnected-(U5I-GND-PadP7) -> GND
- U5 pad P9: unconnected-(U5I-GND-PadP9) -> GND
- U5 pad R1: unconnected-(U5F-IO_L20P_T3_35-PadR1) -> /FPGA/FPGA 3/BA1
- U5 pad R10: unconnected-(U5I-GND-PadR10) -> GND
- U5 pad R12: unconnected-(U5I-GND-PadR12) -> GND
- U5 pad R20: unconnected-(U5I-GND-PadR20) -> GND
- U5 pad R5: unconnected-(U5E-VCCO_34-PadR5) -> /FPGA/FPGA 3/1V35_FD
- U5 pad R8: unconnected-(U5I-GND-PadR8) -> GND
- U5 pad T1: unconnected-(U5E-IO_L1P_T0_34-PadT1) -> /FPGA/FPGA 3/A13
- U5 pad T11: unconnected-(U5I-GND-PadT11) -> GND
- U5 pad T17: unconnected-(U5I-GND-PadT17) -> GND
- U5 pad T2: unconnected-(U5E-VCCO_34-PadT2) -> /FPGA/FPGA 3/1V35_FD
- U5 pad T3: unconnected-(U5E-IO_0_34-PadT3) -> /FPGA/FPGA 3/RESETn
- U5 pad T7: unconnected-(U5I-GND-PadT7) -> GND
- U5 pad T9: unconnected-(U5I-GND-PadT9) -> GND
- U5 pad U1: unconnected-(U5E-IO_L1N_T0_34-PadU1) -> /FPGA/FPGA 3/A14
- U5 pad U14: unconnected-(U5I-GND-PadU14) -> GND
- U5 pad U4: unconnected-(U5I-GND-PadU4) -> GND
- U5 pad V1: unconnected-(U5I-GND-PadV1) -> GND
- U5 pad V11: unconnected-(U5I-GND-PadV11) -> GND
- U5 pad V21: unconnected-(U5I-GND-PadV21) -> GND
- U5 pad V4: unconnected-(U5E-IO_L12P_T1_MRCC_34-PadV4) -> Net-(U5E-IO_L12P_T1_MRCC_34)
- U5 pad V6: unconnected-(U5E-VCCO_34-PadV6) -> /FPGA/FPGA 3/1V35_FD
- U5 pad W18: unconnected-(U5I-GND-PadW18) -> GND
- U5 pad W3: unconnected-(U5E-VCCO_34-PadW3) -> /FPGA/FPGA 3/1V35_FD
- U5 pad W4: unconnected-(U5E-IO_L12N_T1_MRCC_34-PadW4) -> Net-(U5E-IO_L12N_T1_MRCC_34)
- U5 pad W8: unconnected-(U5I-GND-PadW8) -> GND
- U5 pad Y15: unconnected-(U5I-GND-PadY15) -> GND
- U5 pad Y5: unconnected-(U5I-GND-PadY5) -> GND
- U6 pad A1: Net-(U6-V_{DDQ}-PadA1) -> /FPGA/FPGA 3/1V35_FD
- U6 pad A2: /FPGA/Memory/DQ13 -> /FPGA/FPGA 3/DQ13
- U6 pad A3: /FPGA/Memory/DQ15 -> /FPGA/FPGA 3/DQ15
- U6 pad A7: /FPGA/Memory/DQ12 -> /FPGA/FPGA 3/DQ12
- U6 pad A8: Net-(U6-V_{DDQ}-PadA1) -> /FPGA/FPGA 3/1V35_FD
- U6 pad B2: Net-(U6-V_{DD}-PadB2) -> /FPGA/FPGA 3/1V35_FD
- U6 pad B7: unconnected-(U6-~{UDQS}-PadB7) -> /FPGA/FPGA 3/UDQS_N
- U6 pad B8: /FPGA/Memory/DQ14 -> /FPGA/FPGA 3/DQ14
- U6 pad C1: Net-(U6-V_{DDQ}-PadA1) -> /FPGA/FPGA 3/1V35_FD
- U6 pad C2: /FPGA/Memory/DQ11 -> /FPGA/FPGA 3/DQ11
- U6 pad C3: /FPGA/Memory/DQ9 -> /FPGA/FPGA 3/DQ9
- U6 pad C7: unconnected-(U6-UDQS-PadC7) -> /FPGA/FPGA 3/UDQS_P
- U6 pad C8: /FPGA/Memory/DQ10 -> /FPGA/FPGA 3/DQ10
- U6 pad C9: Net-(U6-V_{DDQ}-PadA1) -> /FPGA/FPGA 3/1V35_FD
- U6 pad D2: Net-(U6-V_{DDQ}-PadA1) -> /FPGA/FPGA 3/1V35_FD
- U6 pad D3: unconnected-(U6-UDM-PadD3) -> /FPGA/FPGA 3/UDM
- U6 pad D7: /FPGA/Memory/DQ8 -> /FPGA/FPGA 3/DQ8
- U6 pad D9: Net-(U6-V_{DD}-PadB2) -> /FPGA/FPGA 3/1V35_FD
- U6 pad E3: /FPGA/Memory/DQ0 -> /FPGA/FPGA 3/DQ0
- U6 pad E7: unconnected-(U6-LDM-PadE7) -> /FPGA/FPGA 3/LDM
- U6 pad E9: Net-(U6-V_{DDQ}-PadA1) -> /FPGA/FPGA 3/1V35_FD
- U6 pad F1: Net-(U6-V_{DDQ}-PadA1) -> /FPGA/FPGA 3/1V35_FD
- U6 pad F2: /FPGA/Memory/DQ2 -> /FPGA/FPGA 3/DQ2
- U6 pad F3: unconnected-(U6-LDQS-PadF3) -> /FPGA/FPGA 3/LDQS_P
- U6 pad F7: /FPGA/Memory/DQ1 -> /FPGA/FPGA 3/DQ1
- U6 pad F8: /FPGA/Memory/DQ3 -> /FPGA/FPGA 3/DQ3
- U6 pad G2: /FPGA/Memory/DQ6 -> /FPGA/FPGA 3/DQ6
- U6 pad G3: unconnected-(U6-~{LDQS}-PadG3) -> /FPGA/FPGA 3/LDQS_N
- U6 pad G7: Net-(U6-V_{DD}-PadB2) -> /FPGA/FPGA 3/1V35_FD
- U6 pad H2: Net-(U6-V_{DDQ}-PadA1) -> /FPGA/FPGA 3/1V35_FD
- U6 pad H3: /FPGA/Memory/DQ4 -> /FPGA/FPGA 3/DQ4
- U6 pad H7: /FPGA/Memory/DQ7 -> /FPGA/FPGA 3/DQ7
- U6 pad H8: /FPGA/Memory/DQ5 -> /FPGA/FPGA 3/DQ5
- U6 pad H9: Net-(U6-V_{DDQ}-PadA1) -> /FPGA/FPGA 3/1V35_FD
- U6 pad J3: unconnected-(U6-~{RAS}-PadJ3) -> /FPGA/FPGA 3/RASn
- U6 pad J7: unconnected-(U6-CK-PadJ7) -> /FPGA/FPGA 3/CKp
- U6 pad K1: unconnected-(U6-ODT-PadK1) -> /FPGA/FPGA 3/ODT
- U6 pad K2: Net-(U6-V_{DD}-PadB2) -> /FPGA/FPGA 3/1V35_FD
- U6 pad K3: unconnected-(U6-~{CAS}-PadK3) -> /FPGA/FPGA 3/CASn
- U6 pad K7: unconnected-(U6-~{CK}-PadK7) -> /FPGA/FPGA 3/CKn
- U6 pad K8: Net-(U6-V_{DD}-PadB2) -> /FPGA/FPGA 3/1V35_FD
- U6 pad K9: unconnected-(U6-CKE-PadK9) -> /FPGA/FPGA 3/CKE
- U6 pad L2: unconnected-(U6-~{CS}-PadL2) -> /FPGA/FPGA 3/CSn
- U6 pad L3: unconnected-(U6-~{WE}-PadL3) -> /FPGA/FPGA 3/WEn
- U6 pad L7: /FPGA/Memory/A10 -> /FPGA/FPGA 3/A10
- U6 pad M2: unconnected-(U6-BA0-PadM2) -> /FPGA/FPGA 3/BA0
- U6 pad M3: unconnected-(U6-BA2-PadM3) -> /FPGA/FPGA 3/BA2
- U6 pad N1: Net-(U6-V_{DD}-PadB2) -> /FPGA/FPGA 3/1V35_FD
- U6 pad N2: /FPGA/Memory/A3 -> /FPGA/FPGA 3/A3
- U6 pad N3: /FPGA/Memory/A0 -> /FPGA/FPGA 3/A0
- U6 pad N7: /FPGA/Memory/A12 -> /FPGA/FPGA 3/A12
- U6 pad N8: unconnected-(U6-BA1-PadN8) -> /FPGA/FPGA 3/BA1
- U6 pad N9: Net-(U6-V_{DD}-PadB2) -> /FPGA/FPGA 3/1V35_FD
- U6 pad P2: /FPGA/Memory/A5 -> /FPGA/FPGA 3/A5
- U6 pad P3: /FPGA/Memory/A2 -> /FPGA/FPGA 3/A2
- U6 pad P7: /FPGA/Memory/A1 -> /FPGA/FPGA 3/A1
- U6 pad P8: /FPGA/Memory/A4 -> /FPGA/FPGA 3/A4
- U6 pad R1: Net-(U6-V_{DD}-PadB2) -> /FPGA/FPGA 3/1V35_FD
- U6 pad R2: /FPGA/Memory/A7 -> /FPGA/FPGA 3/A7
- U6 pad R3: /FPGA/Memory/A9 -> /FPGA/FPGA 3/A9
- U6 pad R7: /FPGA/Memory/A11 -> /FPGA/FPGA 3/A11
- U6 pad R8: /FPGA/Memory/A6 -> /FPGA/FPGA 3/A6
- U6 pad R9: Net-(U6-V_{DD}-PadB2) -> /FPGA/FPGA 3/1V35_FD
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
